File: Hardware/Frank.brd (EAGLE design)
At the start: 66 x 67.2 mm, 24 parts, among them U2 PRO_MICRO_C

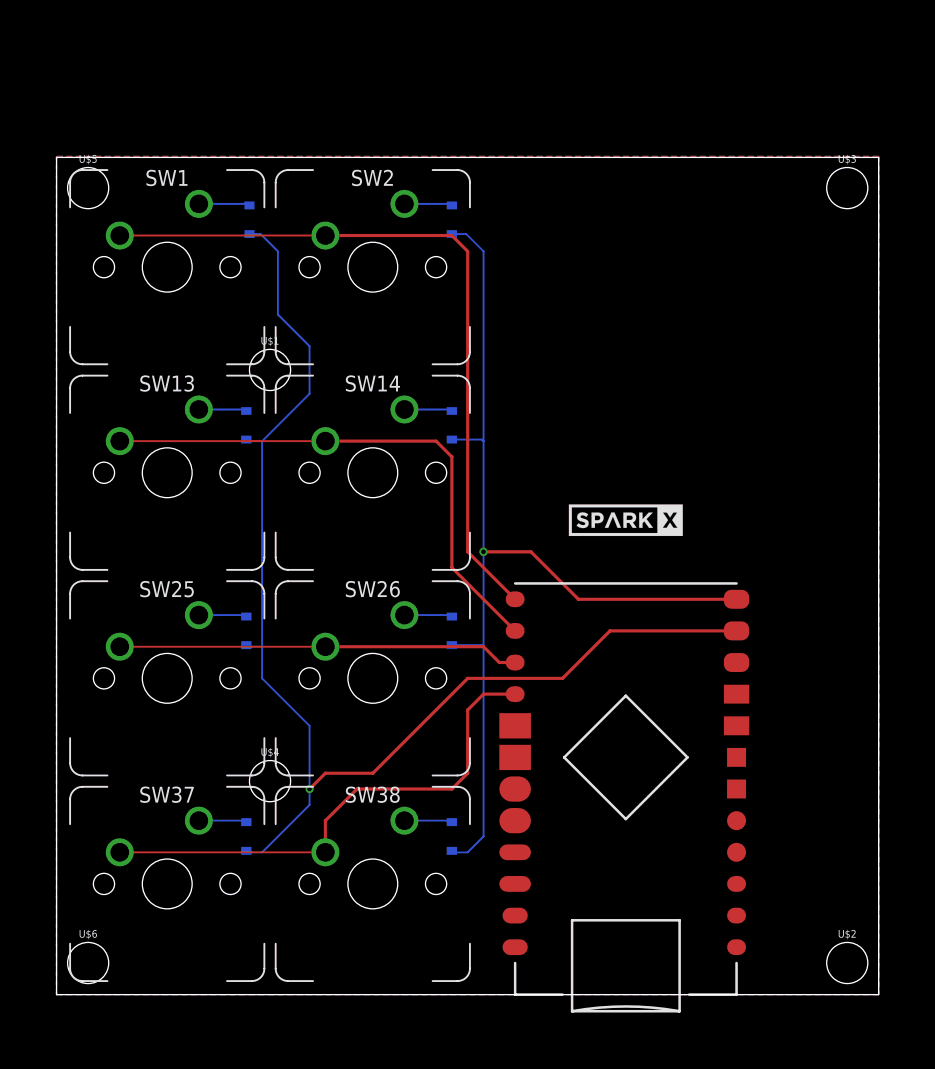
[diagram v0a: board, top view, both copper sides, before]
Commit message: Updates to Pro Micro and Frank
"Castellated" library '1x12CASTELLATED' and 'PRO_MICRO_C' footprints updated and 'PRO_MICRO_C' device updated.

Pro Micro C got uniform drill/ring sizing + added plated holes to outside in place of drills

Frank got 1U Keycap standard switch spacing and updated Pro Micro footprint.
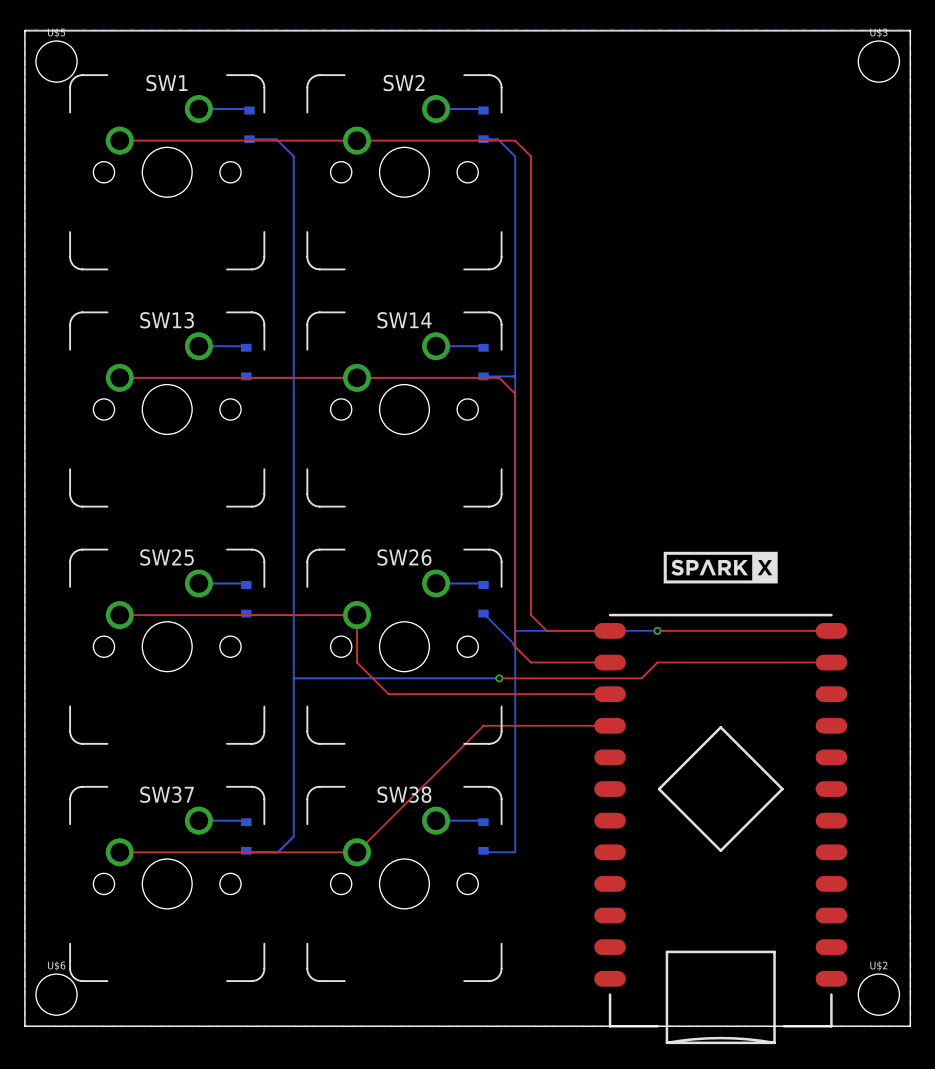
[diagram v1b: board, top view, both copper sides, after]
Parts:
- removed U$1, U$4: (no value), SparkFun-Hardware:STAND-OFF
- moved U$3 10.5 mm to (66.0, 74.9)
- moved U$5 10.5 mm to (0.00, 74.9)
- moved U$7 8.52 mm to (53.3, 34.3)
- moved SW2 8.03 mm to (27.9, 66.0)
- moved U2 8.03 mm to (53.3, 14.0)
- moved D3 8.03 mm to (34.3, 69.8)
- moved SW1 7.62 mm to (8.89, 66.0)
- moved D2 7.62 mm to (15.5, 69.8)
- moved SW14 5.68 mm to (27.9, 47.0)
- moved D14 5.68 mm to (34.3, 50.8)
- moved SW13 5.08 mm to (8.89, 47.0)
- moved D1 5.08 mm to (15.2, 50.8)
- moved U$2 3.59 mm to (66.0, 0.00)
- moved SW26 3.59 mm to (27.9, 27.9)
- moved U$6 3.59 mm to (0.00, 0.00)
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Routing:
- net ROW1: track 58.0 -> 77.3 mm
- net ROW2: track 43.3 -> 60.7 mm
- net COL1: track 100.4 -> 114.6 mm
- net COL2: track 80.3 -> 93.3 mm
- net ROW4: track 32.3 -> 44.2 mm
- net ROW3: track 41.5 -> 43.6 mm
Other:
- board size 66 x 67.2 mm -> 71.1 x 79.9 mm
